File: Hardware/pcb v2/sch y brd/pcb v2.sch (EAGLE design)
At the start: 58 parts, among them J1 AVR_SPI_PRG_6PTH, J2 1981584-1, J3 HDMI, J4 JST-3, J5 HDMI, J6 FEMALE 2x3, J7 2X6 FEMALE, Q1 PMBT3904, Q2 PMBT3904, U1 ATMEGA328P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

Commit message: bom y cambios menores en la pcb
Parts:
- C13: value 100uF -> 10uF; device rcl:C-USC1206 -> rcl:C-USC0805
- R13: value 1K -> 1k
- R15: device rcl:R-US_R0805 -> rcl:R-US_R0603
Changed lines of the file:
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@@
 <part name="Q2" library="diego" deviceset="PMBT3904" device=""/>
 <part name="R12" library="rcl" deviceset="R-US_" device="R0805" value="1k"/>
-<part name="R13" library="rcl" deviceset="R-US_" device="R0805" value="1K"/>
+<part name="R13" library="rcl" deviceset="R-US_" device="R0805" value="1k"/>
 <part name="P+7" library="supply1" deviceset="+5V" device=""/>
 <part name="C17" library="rcl" deviceset="C-US" device="C0805" value="1uF"/>
@@
 <part name="S1" library="SparkFun-Electromechanical" deviceset="SWITCH-MOMENTARY-2" device="SMD"/>
 <part name="GND24" library="supply1" deviceset="GND" device=""/>
-<part name="R15" library="rcl" deviceset="R-US_" device="R0805" value="10k"/>
+<part name="R15" library="rcl" deviceset="R-US_" device="R0603" value="10k"/>
 <part name="P+10" library="supply1" deviceset="+5V" device=""/>
 <part name="C8" library="rcl" deviceset="C-US" device="C0805" value="10uF"/>
@@
 <part name="Y2" library="crystal" deviceset="MC-306" device=""/>
 <part name="C14" library="rcl" deviceset="CPOL-US" device="UD-10X10" value="1200uF"/>
-<part name="C13" library="rcl" deviceset="C-US" device="C1206" value="100uF"/>
+<part name="C13" library="rcl" deviceset="C-US" device="C0805" value="10uF"/>
 <part name="C15" library="rcl" deviceset="CPOL-US" device="UD-10X10" value="1200uF"/>
 <part name="C16" library="rcl" deviceset="CPOL-US" device="UD-5X5,8" value="10uF"/>

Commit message: cambio de boton
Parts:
- S1: value SWITCH-MOMENTARY-2SMD -> PULSADOR-SPST-SMD-1-3-4; device SparkFun-Electromechanical:SWITCH-MOMENTARY-2SMD -> partes v2:PULSADOR-SPST-SMD-1-3-4
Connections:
- net BOTON: now also S1.P$1; no longer S1.1
- net GND: now also S1.P$2; no longer S1.2
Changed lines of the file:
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@@
 <part name="GND16" library="supply1" deviceset="GND" device=""/>
 <part name="R8" library="rcl" deviceset="R-US_" device="R0603" value="10k"/>
-<part name="S1" library="SparkFun-Electromechanical" deviceset="SWITCH-MOMENTARY-2" device="SMD"/>
+<part name="S1" library="partes v2" deviceset="PULSADOR-SPST" device="-SMD-1-3-4" value="PULSADOR-SPST-SMD-1-3-4"/>
 <part name="GND24" library="supply1" deviceset="GND" device=""/>
 <part name="R15" library="rcl" deviceset="R-US_" device="R0603" value="10k"/>
@@
 </segment>
 <segment>
-<pinref part="S1" gate="G$1" pin="2"/>
+<pinref part="S1" gate="G$1" pin="P$2"/>
 <pinref part="GND24" gate="1" pin="GND"/>
 <wire x1="441.96" y1="88.9" x2="441.96" y2="83.82" width="0.1524" layer="91"/>
@@
 <net name="BOTON" class="0">
 <segment>
-<pinref part="S1" gate="G$1" pin="1"/>
+<pinref part="S1" gate="G$1" pin="P$1"/>
 <pinref part="R15" gate="G$1" pin="1"/>
 <wire x1="441.96" y1="99.06" x2="441.96" y2="101.6" width="0.1524" layer="91"/>

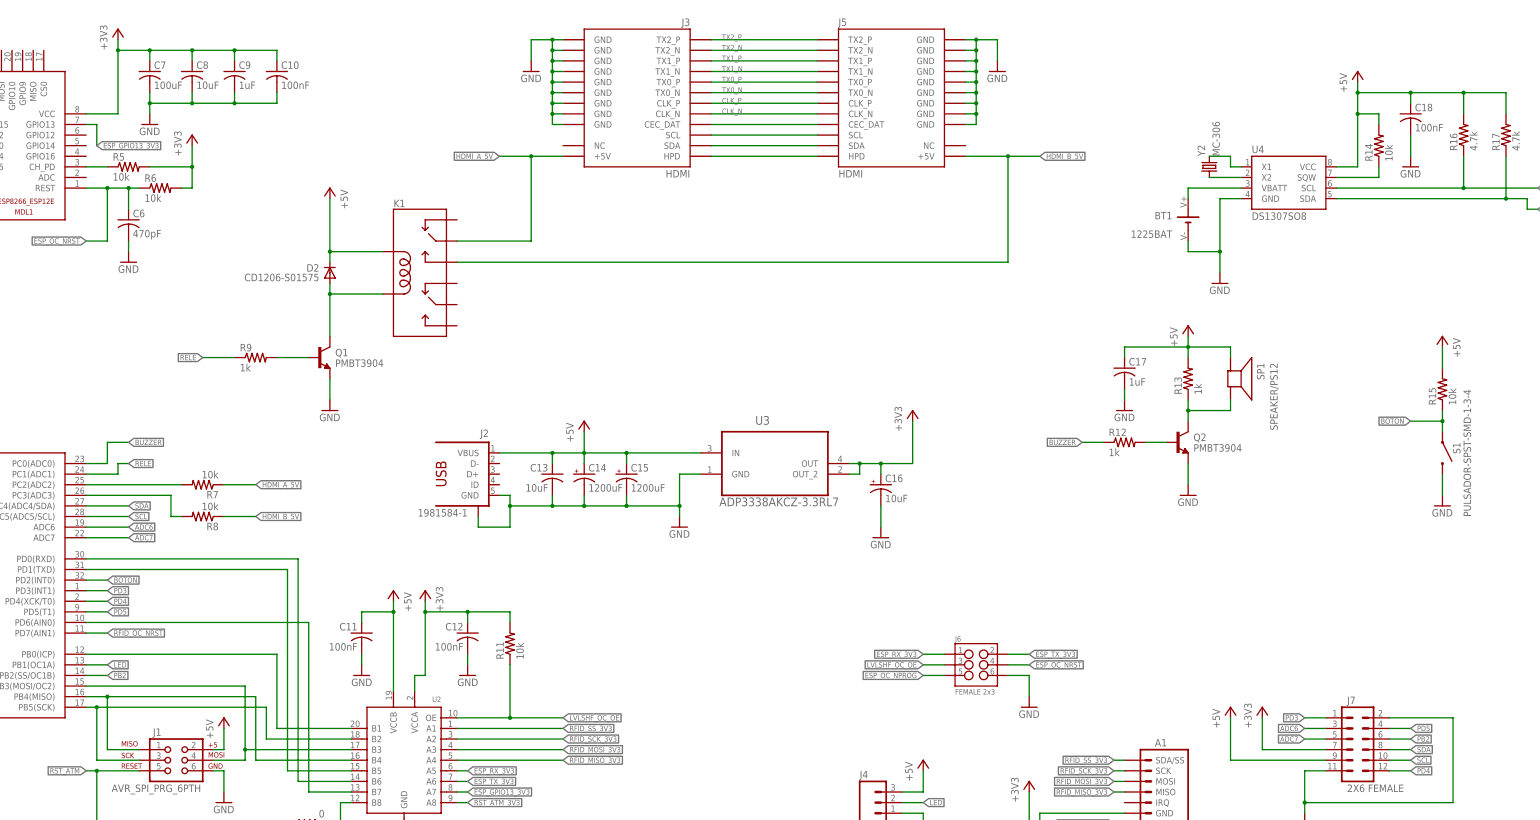
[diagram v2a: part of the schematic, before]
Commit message: Boton conectado al esp
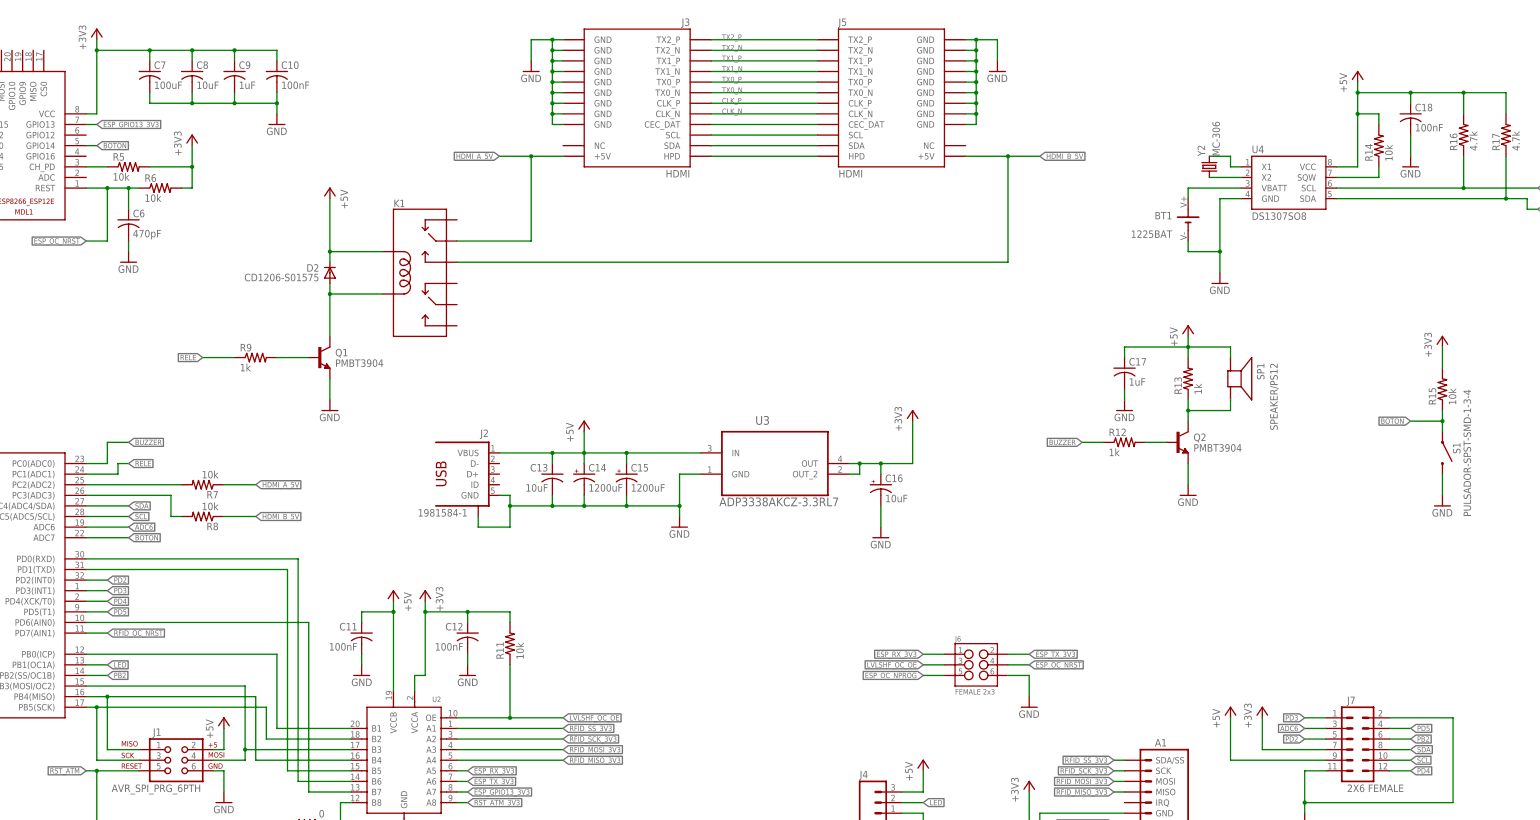
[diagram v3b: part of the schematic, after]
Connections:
- removed net ADC7: J7.5, U1.ADC7
- new net PD2: J7.5, U1.PD2(INT0)
- net +3V3: now also R15.2
- net +5V: no longer R15.2
- net BOTON: now also MDL1.GPIO14, U1.ADC7; no longer U1.PD2(INT0)
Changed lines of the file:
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@@
 <part name="GND24" library="supply1" deviceset="GND" device=""/>
 <part name="R15" library="rcl" deviceset="R-US_" device="R0603" value="10k"/>
-<part name="P+10" library="supply1" deviceset="+5V" device=""/>
 <part name="C8" library="rcl" deviceset="C-US" device="C0805" value="10uF"/>
 <part name="C9" library="rcl" deviceset="C-US" device="C0805" value="1uF"/>
@@
 <part name="GND18" library="supply1" deviceset="GND" device=""/>
 <part name="BT1" library="partes v2" deviceset="1225BAT" device=""/>
+<part name="+3V1" library="supply1" deviceset="+3V3" device=""/>
 </parts>
 <sheets>
@@
 <instance part="C12" gate="G$1" x="208.28" y="50.8" rot="MR0"/>
 <instance part="MDL1" gate="G$1" x="93.98" y="165.1" rot="R180"/>
-<instance part="+3V32" gate="G$1" x="124.46" y="195.58"/>
+<instance part="+3V32" gate="G$1" x="119.38" y="195.58"/>
 <instance part="GND2" gate="1" x="55.88" y="144.78"/>
 <instance part="+3V31" gate="G$1" x="53.34" y="198.12"/>
@@
 <instance part="C7" gate="G$1" x="132.08" y="185.42"/>
 <instance part="C10" gate="G$1" x="162.56" y="185.42"/>
-<instance part="GND6" gate="1" x="132.08" y="172.72"/>
+<instance part="GND6" gate="1" x="162.56" y="172.72"/>
 <instance part="C6" gate="G$1" x="127" y="149.86"/>
 <instance part="GND5" gate="1" x="127" y="139.7"/>
@@
 <instance part="GND24" gate="1" x="441.96" y="81.28"/>
 <instance part="R15" gate="G$1" x="441.96" y="109.22" rot="R90"/>
-<instance part="P+10" gate="1" x="441.96" y="121.92" rot="MR0"/>
 <instance part="C8" gate="G$1" x="142.24" y="185.42"/>
 <instance part="C9" gate="G$1" x="152.4" y="185.42"/>
@@
 <attribute name="VALUE" x="377.19" y="147.32" size="1.778" layer="96" rot="R180"/>
 </instance>
+<instance part="+3V1" gate="G$1" x="441.96" y="121.92"/>
 </instances>
 <busses>
@@
 <wire x1="55.88" y1="149.86" x2="55.88" y2="175.26" width="0.1524" layer="91"/>
 <wire x1="55.88" y1="175.26" x2="83.82" y2="175.26" width="0.1524" layer="91"/>
-</segment>
-<segment>
-<pinref part="GND6" gate="1" pin="GND"/>
-<pinref part="C7" gate="G$1" pin="2"/>
-<wire x1="132.08" y1="175.26" x2="132.08" y2="177.8" width="0.1524" layer="91"/>
-<wire x1="132.08" y1="177.8" x2="132.08" y2="180.34" width="0.1524" layer="91"/>
-<wire x1="132.08" y1="177.8" x2="142.24" y2="177.8" width="0.1524" layer="91"/>
-<junction x="132.08" y="177.8"/>
-<pinref part="C10" gate="G$1" pin="2"/>
-<wire x1="142.24" y1="177.8" x2="152.4" y2="177.8" width="0.1524" layer="91"/>
-<wire x1="152.4" y1="177.8" x2="162.56" y2="177.8" width="0.1524" layer="91"/>
-<wire x1="162.56" y1="177.8" x2="162.56" y2="180.34" width="0.1524" layer="91"/>
-<pinref part="C8" gate="G$1" pin="2"/>
-<wire x1="142.24" y1="180.34" x2="142.24" y2="177.8" width="0.1524" layer="91"/>
-<junction x="142.24" y="177.8"/>
-<pinref part="C9" gate="G$1" pin="2"/>
-<wire x1="152.4" y1="180.34" x2="152.4" y2="177.8" width="0.1524" layer="91"/>
-<junction x="152.4" y="177.8"/>
 </segment>
 <segment>
@@
 <wire x1="345.44" y1="7.62" x2="365.76" y2="7.62" width="0.1524" layer="91"/>
 </segment>
+<segment>
+<pinref part="C7" gate="G$1" pin="2"/>
+<wire x1="132.08" y1="177.8" x2="132.08" y2="180.34" width="0.1524" layer="91"/>
+<wire x1="132.08" y1="177.8" x2="142.24" y2="177.8" width="0.1524" layer="91"/>
+<pinref part="C10" gate="G$1" pin="2"/>
+<wire x1="142.24" y1="177.8" x2="152.4" y2="177.8" width="0.1524" layer="91"/>
+<wire x1="152.4" y1="177.8" x2="162.56" y2="177.8" width="0.1524" layer="91"/>
+<wire x1="162.56" y1="177.8" x2="162.56" y2="180.34" width="0.1524" layer="91"/>
+<pinref part="C8" gate="G$1" pin="2"/>
+<wire x1="142.24" y1="180.34" x2="142.24" y2="177.8" width="0.1524" layer="91"/>
+<junction x="142.24" y="177.8"/>
+<pinref part="C9" gate="G$1" pin="2"/>
+<wire x1="152.4" y1="180.34" x2="152.4" y2="177.8" width="0.1524" layer="91"/>
+<junction x="152.4" y="177.8"/>
+<pinref part="GND6" gate="1" pin="GND"/>
+<wire x1="162.56" y1="175.26" x2="162.56" y2="177.8" width="0.1524" layer="91"/>
+<junction x="162.56" y="177.8"/>
+</segment>
 </net>
 <net name="+5V" class="0">
@@
 </segment>
 <segment>
-<pinref part="P+10" gate="1" pin="+5V"/>
-<pinref part="R15" gate="G$1" pin="2"/>
-<wire x1="441.96" y1="119.38" x2="441.96" y2="114.3" width="0.1524" layer="91"/>
-</segment>
-<segment>
 <wire x1="312.42" y1="12.7" x2="317.5" y2="12.7" width="0.1524" layer="91"/>
 <wire x1="317.5" y1="12.7" x2="317.5" y2="17.78" width="0.1524" layer="91"/>
@@
 <pinref part="+3V32" gate="G$1" pin="+3V3"/>
 <pinref part="MDL1" gate="G$1" pin="VCC"/>
-<wire x1="124.46" y1="193.04" x2="124.46" y2="190.5" width="0.1524" layer="91"/>
-<wire x1="124.46" y1="190.5" x2="124.46" y2="175.26" width="0.1524" layer="91"/>
-<wire x1="124.46" y1="175.26" x2="116.84" y2="175.26" width="0.1524" layer="91"/>
-<wire x1="124.46" y1="190.5" x2="132.08" y2="190.5" width="0.1524" layer="91"/>
-<junction x="124.46" y="190.5"/>
+<wire x1="119.38" y1="193.04" x2="119.38" y2="190.5" width="0.1524" layer="91"/>
+<wire x1="119.38" y1="190.5" x2="119.38" y2="175.26" width="0.1524" layer="91"/>
+<wire x1="119.38" y1="175.26" x2="116.84" y2="175.26" width="0.1524" layer="91"/>
+<wire x1="119.38" y1="190.5" x2="132.08" y2="190.5" width="0.1524" layer="91"/>
+<junction x="119.38" y="190.5"/>
 <pinref part="C10" gate="G$1" pin="1"/>
 <wire x1="132.08" y1="190.5" x2="142.24" y2="190.5" width="0.1524" layer="91"/>
@@
 <pinref part="+3V36" gate="G$1" pin="+3V3"/>
 </segment>
+<segment>
+<pinref part="+3V1" gate="G$1" pin="+3V3"/>
+<pinref part="R15" gate="G$1" pin="2"/>
+<wire x1="441.96" y1="119.38" x2="441.96" y2="114.3" width="0.1524" layer="91"/>
+</segment>
 </net>
 <net name="N$8" class="0">
@@
 </segment>
 <segment>
-<pinref part="U1" gate="G$1" pin="PD2(INT0)"/>
-<wire x1="116.84" y1="63.5" x2="121.92" y2="63.5" width="0.1524" layer="91"/>
-<label x="121.92" y="63.5" size="1.27" layer="95" xref="yes"/>
+<pinref part="MDL1" gate="G$1" pin="GPIO14"/>
+<wire x1="116.84" y1="167.64" x2="119.38" y2="167.64" width="0.1524" layer="91"/>
+<label x="119.38" y="167.64" size="1.27" layer="95" xref="yes"/>
+</segment>
+<segment>
+<pinref part="U1" gate="G$1" pin="ADC7"/>
+<wire x1="116.84" y1="73.66" x2="127" y2="73.66" width="0.1524" layer="91"/>
+<label x="127" y="73.66" size="1.27" layer="95" xref="yes"/>
 </segment>
 </net>
@@
 <wire x1="414.02" y1="27.94" x2="408.94" y2="27.94" width="0.1524" layer="91"/>
 <label x="408.94" y="27.94" size="1.27" layer="95" rot="R180" xref="yes"/>
-</segment>
-</net>
-<net name="ADC7" class="0">
-<segment>
-<pinref part="U1" gate="G$1" pin="ADC7"/>
-<wire x1="116.84" y1="73.66" x2="127" y2="73.66" width="0.1524" layer="91"/>
-<label x="127" y="73.66" size="1.27" layer="95" xref="yes"/>
-</segment>
-<segment>
-<pinref part="J7" gate="G$1" pin="5"/>
-<wire x1="414.02" y1="25.4" x2="408.94" y2="25.4" width="0.1524" layer="91"/>
-<label x="408.94" y="25.4" size="1.27" layer="95" rot="R180" xref="yes"/>
 </segment>
 </net>
@@
 <pinref part="MDL1" gate="G$1" pin="GPIO13"/>
 <wire x1="116.84" y1="172.72" x2="119.38" y2="172.72" width="0.1524" layer="91"/>
-<wire x1="119.38" y1="172.72" x2="119.38" y2="167.64" width="0.1524" layer="91"/>
-<label x="119.38" y="167.64" size="1.27" layer="95" xref="yes"/>
+<label x="119.38" y="172.72" size="1.27" layer="95" xref="yes"/>
 </segment>
 <segment>
@@
 </segment>
 </net>
+<net name="PD2" class="0">
+<segment>
+<pinref part="U1" gate="G$1" pin="PD2(INT0)"/>
+<wire x1="116.84" y1="63.5" x2="121.92" y2="63.5" width="0.1524" layer="91"/>
+<label x="121.92" y="63.5" size="1.27" layer="95" xref="yes"/>
+</segment>
+<segment>
+<pinref part="J7" gate="G$1" pin="5"/>
+<wire x1="414.02" y1="25.4" x2="408.94" y2="25.4" width="0.1524" layer="91"/>
+<label x="408.94" y="25.4" size="1.27" layer="95" rot="R180" xref="yes"/>
+</segment>
+</net>
